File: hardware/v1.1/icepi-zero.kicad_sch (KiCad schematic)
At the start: 26 parts, among them J1 Conn_02x20_Counter_Clockwise, SW1 SW_Push, SW2 SW_Push, U1 ECP5U_12_CABGA256

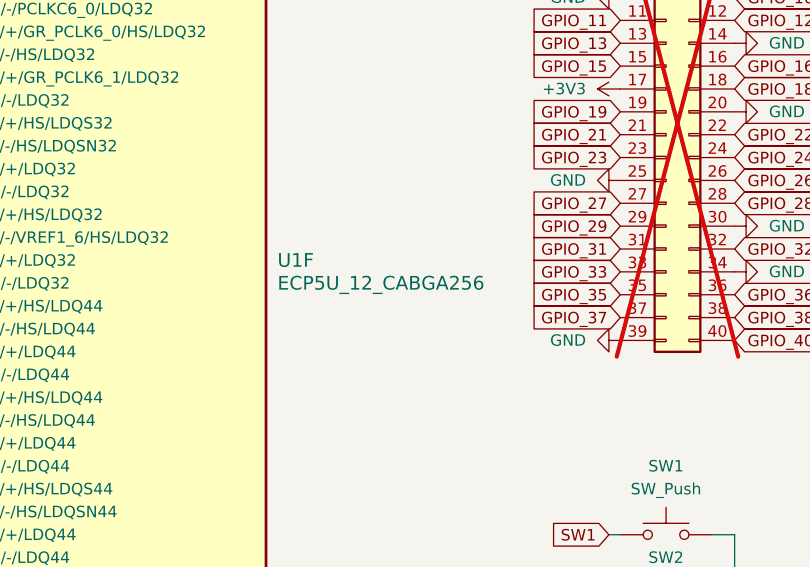
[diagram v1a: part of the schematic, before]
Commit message: Clean up the design by a bit
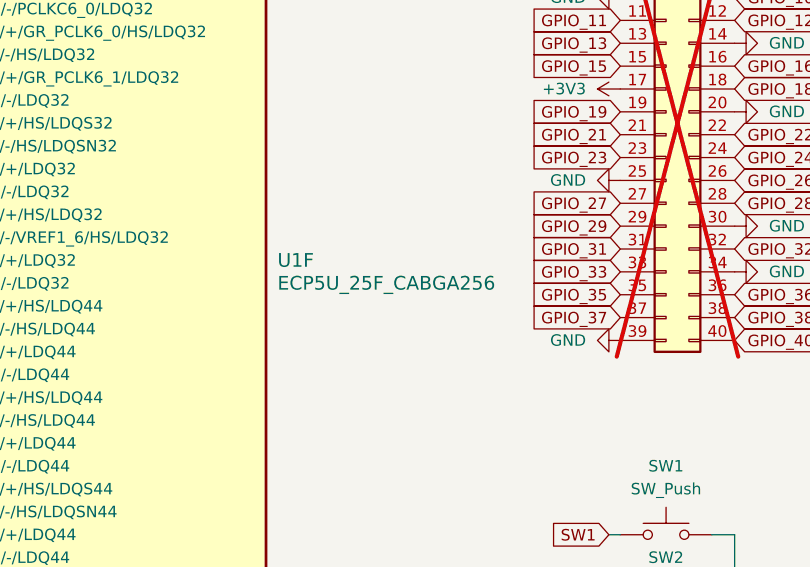
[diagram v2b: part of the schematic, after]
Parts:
- U1: value ECP5U_12_CABGA256 -> ECP5U_25F_CABGA256
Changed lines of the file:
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@@
 			)
 		)
-		(property "Value" "ECP5U_12_CABGA256"
+		(property "Value" "ECP5U_25F_CABGA256"
 			(at 91.44 138.4299 0)
 			(effects

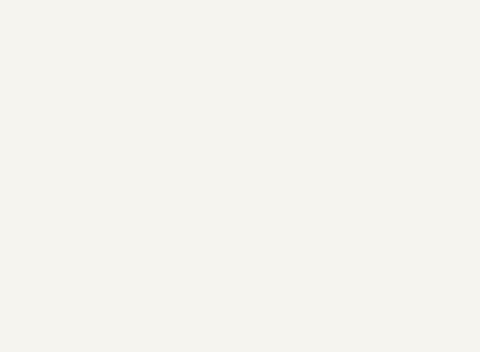
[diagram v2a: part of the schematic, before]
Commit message: OSHWA cerification :yay: and pinout diagram
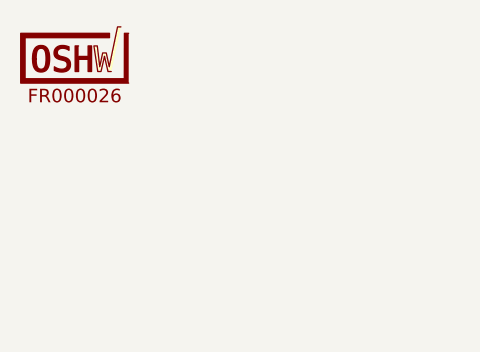
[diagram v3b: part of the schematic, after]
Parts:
- added LOGO1: ~, oshw:OSHW-Certification-Mark-Logo_6x3mm_SilkScreen, symbol oshw:OSHW_Certification_Mark_Stacked_Medium
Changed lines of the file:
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@@
+	)
+	(symbol
+		(lib_id "oshw:OSHW_Certification_Mark_Stacked_Medium")
+		(at 24.13 20.32 0)
+		(unit 1)
+		(exclude_from_sim no)
+		(in_bom no)
+		(on_board yes)
+		(dnp no)
+		(fields_autoplaced yes)
+		(property "Reference" "LOGO1"
+			(at 24.13 20.32 0)
+			(effects
+				(font
+					(size 1.27 1.27)
+				)
+				(hide yes)
+			)
+		)
+		(property "Value" "~"
+			(at 24.13 20.32 0)
+			(effects
+				(font
+					(size 1.27 1.27)
+				)
+				(hide yes)
+			)
+		)
+		(property "Footprint" "oshw:OSHW-Certification-Mark-Logo_6x3mm_SilkScreen"
+			(at 24.13 20.32 0)
+			(effects
+				(font
+					(size 1.27 1.27)
+				)
+				(hide yes)
+			)
+		)
+		(property "Datasheet" ""
+			(at 24.13 20.32 0)
+			(effects
+				(font
+					(size 1.27 1.27)
+				)
+				(hide yes)
+			)
+		)
+		(property "Description" "OSHW Certification Mark, Stacked"
+			(at 24.13 20.32 0)
+			(effects
+				(font
+					(size 1.27 1.27)
+				)
+				(hide yes)
+			)
+		)
+		(instances
+			(project ""
+				(path "/f88da08e-cf42-4d03-a08f-3f602fe6658d"
+					(reference "LOGO1")
+					(unit 1)
+				)
+			)
+		)
 	)
 	(symbol

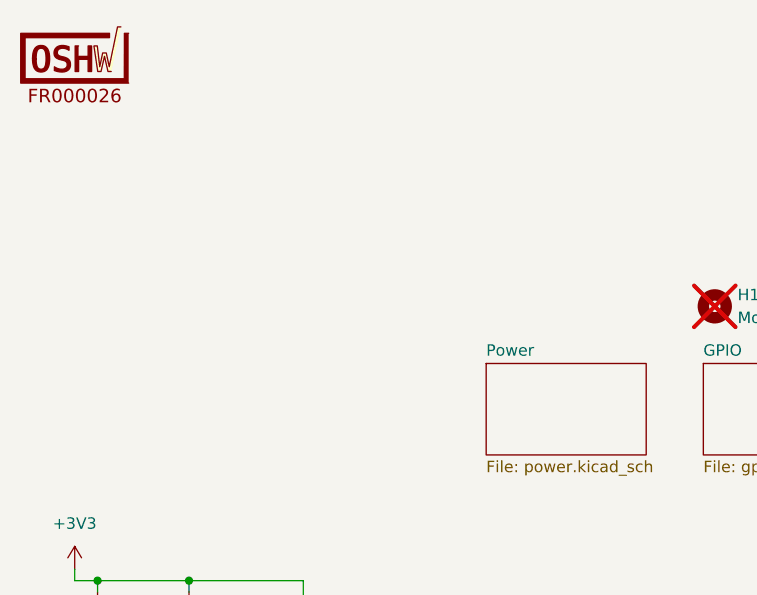
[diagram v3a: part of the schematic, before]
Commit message: Fix wrong dates on shematic and pcb sheet
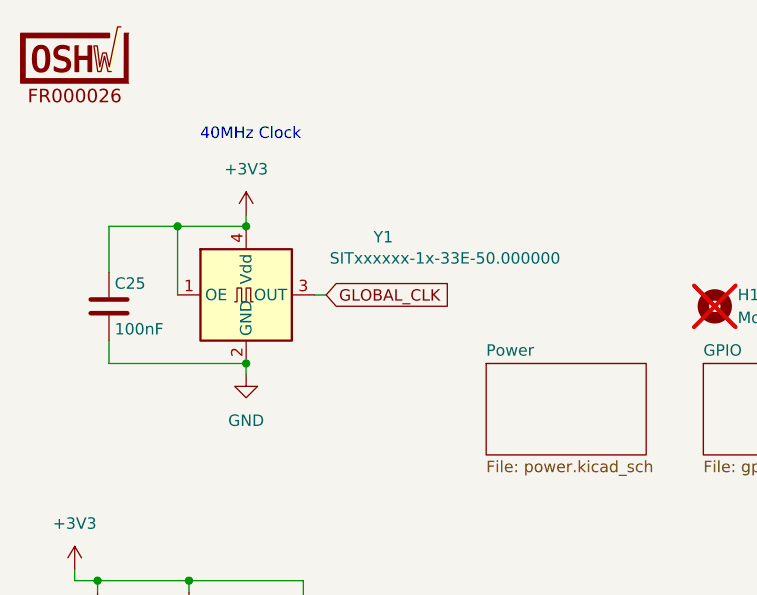
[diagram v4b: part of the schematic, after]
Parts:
- added C25: 100nF, Capacitor_SMD:C_0402_1005Metric, symbol Device:C
- added Y1: SITxxxxxx-1x-33E-50.000000, Oscillator:Oscillator_SMD_SiT_PQFN-4Pin_2.5x2.0mm, symbol Oscillator:SiT8008xx-1x-xxE
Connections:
- net +3V3: now also C25.1, Y1.1 (OE), Y1.4 (Vdd)
- net GLOBAL_CLK: now also Y1.3 (OUT)
- net GND: now also C25.2, Y1.2 (GND)
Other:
- note added: "40MHz Clock"

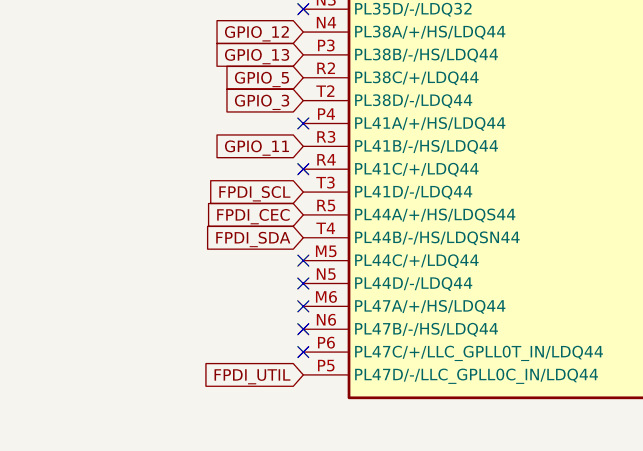
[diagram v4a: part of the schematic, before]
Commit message: Fix pin assignment errors and schematic lable naming mismatch between versions
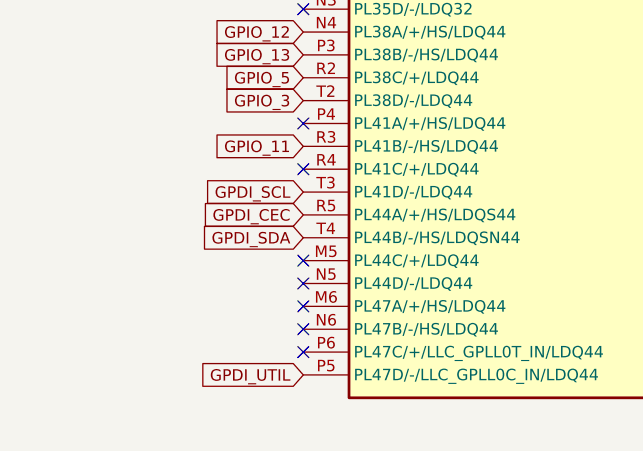
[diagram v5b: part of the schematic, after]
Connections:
- net FPDI_CEC renamed GPDI_CEC
- net FPDI_SCL renamed GPDI_SCL
- net FPDI_SDA renamed GPDI_SDA
- net FPDI_UTIL renamed GPDI_UTIL
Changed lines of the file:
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@@
 		)
 	)
-	(global_label "FPDI_SDA"
+	(global_label "GPDI_SDA"
 		(shape input)
 		(at 49.53 163.83 180)
@@
 		)
 	)
-	(global_label "FPDI_CEC"
+	(global_label "GPDI_CEC"
 		(shape input)
 		(at 49.53 161.29 180)
@@
 		)
 	)
-	(global_label "FPDI_UTIL"
+	(global_label "GPDI_UTIL"
 		(shape input)
 		(at 49.53 179.07 180)
@@
 		)
 	)
-	(global_label "FPDI_SCL"
+	(global_label "GPDI_SCL"
 		(shape input)
 		(at 49.53 158.75 180)

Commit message: Replace unavaliable part
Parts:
- SW1, SW2: LCSC Part # C2689695 -> C2764561
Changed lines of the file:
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@@
 			)
 		)
-		(property "LCSC Part #" "C2689695"
+		(property "LCSC Part #" "C2764561"
 			(at 134.62 176.53 0)
 			(effects
@@
 			)
 		)
-		(property "LCSC Part #" "C2689695"
+		(property "LCSC Part #" "C2764561"
 			(at 134.62 166.37 0)
 			(effects

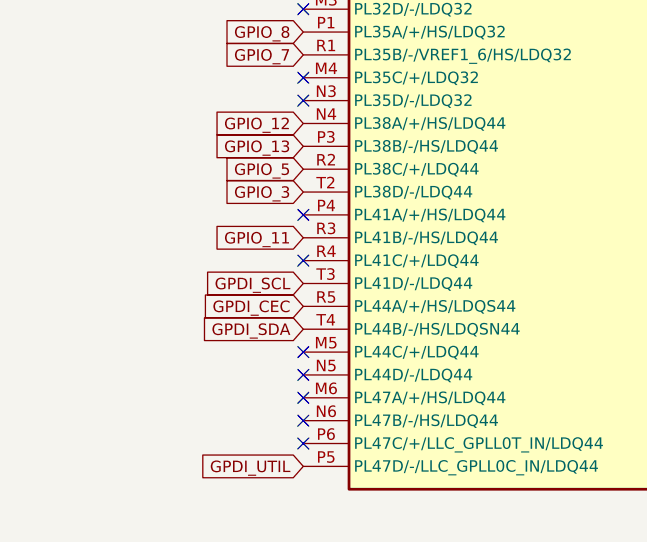
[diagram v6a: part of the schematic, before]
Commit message: Increase pad spacing to 1.9mm and change SCL name to SCK
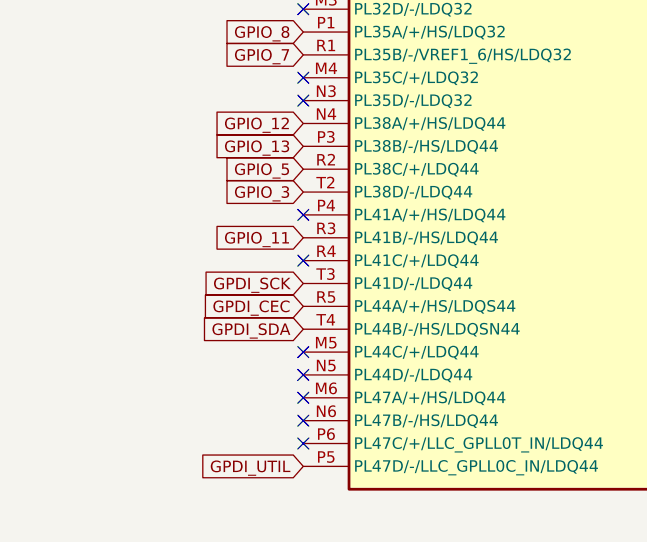
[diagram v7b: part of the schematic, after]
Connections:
- net GPDI_SCL renamed GPDI_SCK
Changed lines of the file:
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@@
 	(title_block
 		(title "Icepi zero")
-		(date "2025-06-06")
+		(date "2025-06-11")
 		(rev "v1.1")
 		(company "Chengyin Yao (cheyao)")
@@
 		)
 	)
-	(global_label "GPDI_SCL"
+	(global_label "GPDI_SCK"
 		(shape input)
 		(at 49.53 158.75 180)

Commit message: Fix typo in filename
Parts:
- SW1, SW2: footprint Button_Switch_SMD:SW_SPST_B3U-1000P -> icepi-lib:switch_button_TS-1088-AR02016; LCSC Part # C2764561 -> C720477
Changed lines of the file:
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@@
 			)
 		)
-		(property "Footprint" "Button_Switch_SMD:SW_SPST_B3U-1000P"
+		(property "Footprint" "icepi-lib:switch_button_TS-1088-AR02016"
 			(at 134.62 171.45 0)
 			(effects
@@
 			)
 		)
-		(property "LCSC Part #" "C2764561"
+		(property "LCSC Part #" "C720477"
 			(at 134.62 176.53 0)
 			(effects
@@
 			)
 		)
-		(property "Footprint" "Button_Switch_SMD:SW_SPST_B3U-1000P"
+		(property "Footprint" "icepi-lib:switch_button_TS-1088-AR02016"
 			(at 134.62 161.29 0)
 			(effects
@@
 			)
 		)
-		(property "LCSC Part #" "C2764561"
+		(property "LCSC Part #" "C720477"
 			(at 134.62 166.37 0)
 			(effects
